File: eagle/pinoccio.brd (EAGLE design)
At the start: 25.4 x 50.8 mm, 71 parts, among them J1 AVR_SPI_PRG_6, J2 AVR_SPI, J3 Switch, J4 Ext Battery, Q1 PFET, U1 MCP73832, U2 TPS78233, U3 ATMEGA16U2, U4 ATMEGA256RFR2, U5 MAX17048, U6 SWITCH, U7 SWITCH, U8 LED-RGB, X1 16MHz, X2 32.768k, X3 16MHz, Y1 ANTENNA2SMD5

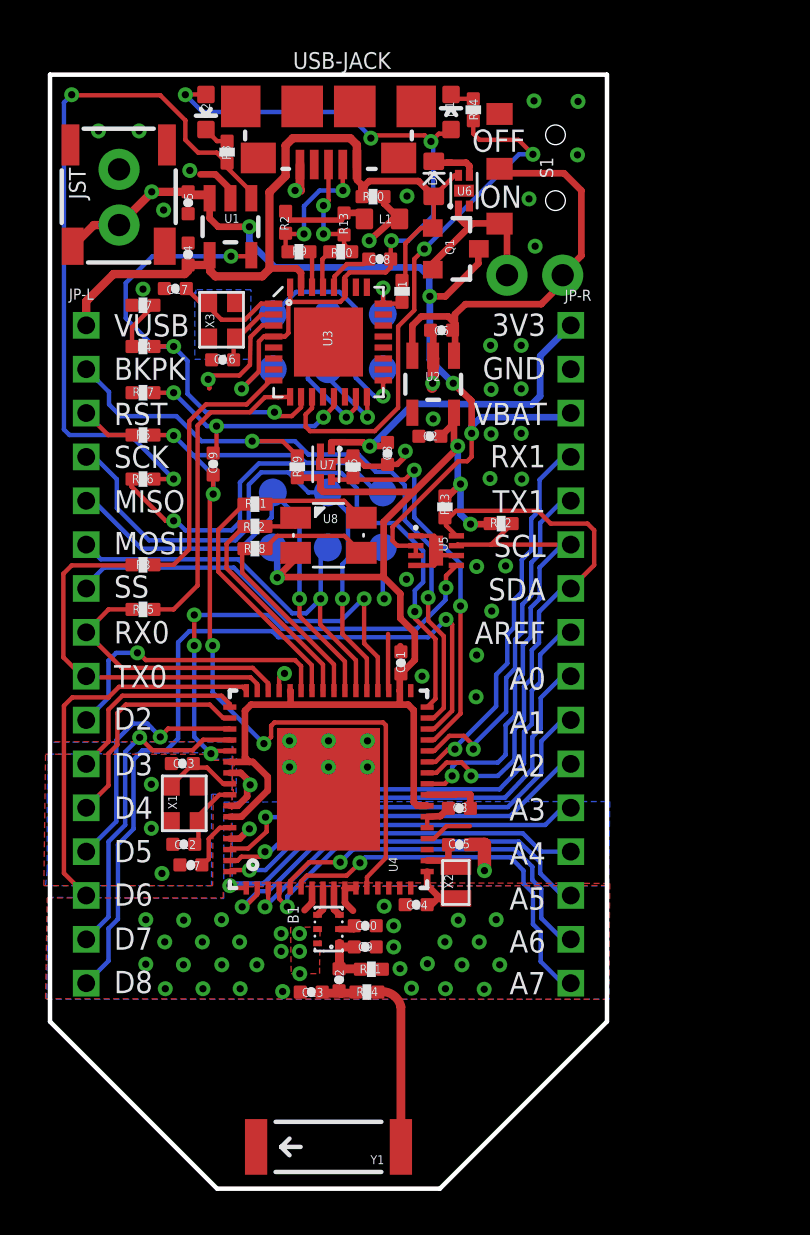
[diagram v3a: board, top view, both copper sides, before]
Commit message: Hardware updates to Scout v1.1
- Add 10k pull-up to reset line (#7)
- Add diode in parallel to 10k pull-up reset resistor (#6)
- Tie second pad on 16U2 crystal to ground (was not connected before)
- Replace LDO with lower-ripple alternative (#8) (STLQ015XX33)
- Add ground tie (0Ω) to pin 2 of balun
- Change all caps in RF signal path to RF-rated C0G/NPO (Murata GRM series)
- Reduce C7 and C8 to 100nF, and make C0G/NPO or X7R (<-Atmel engineer, could be 1.0µF instead)
- Consider adding the SE2438T Front-end module (FEM) amplifier
- Consider ferrite bead between digital and analog VDD lines
- Consider decoupling of 0.1µF on all VDD/GND pin pairs
- Move to a four layer board (GND/VDD in the middle two layers, signals on outer two)
- Add VBUS voltage check (with voltage divider to kick 5v -> 3.3v) into RFR2 and 16U2 input
- Change 16U2 to be powered via VBAT always, instead of off of VUSB
- Tie 16U2 pin to RFR2 pin, to notify RFR2 when serial port is opened
- Add series resistor to 16U2->RST line, removing existing reset circuit
- Remove load switch from VUSB, as it's now unneeded
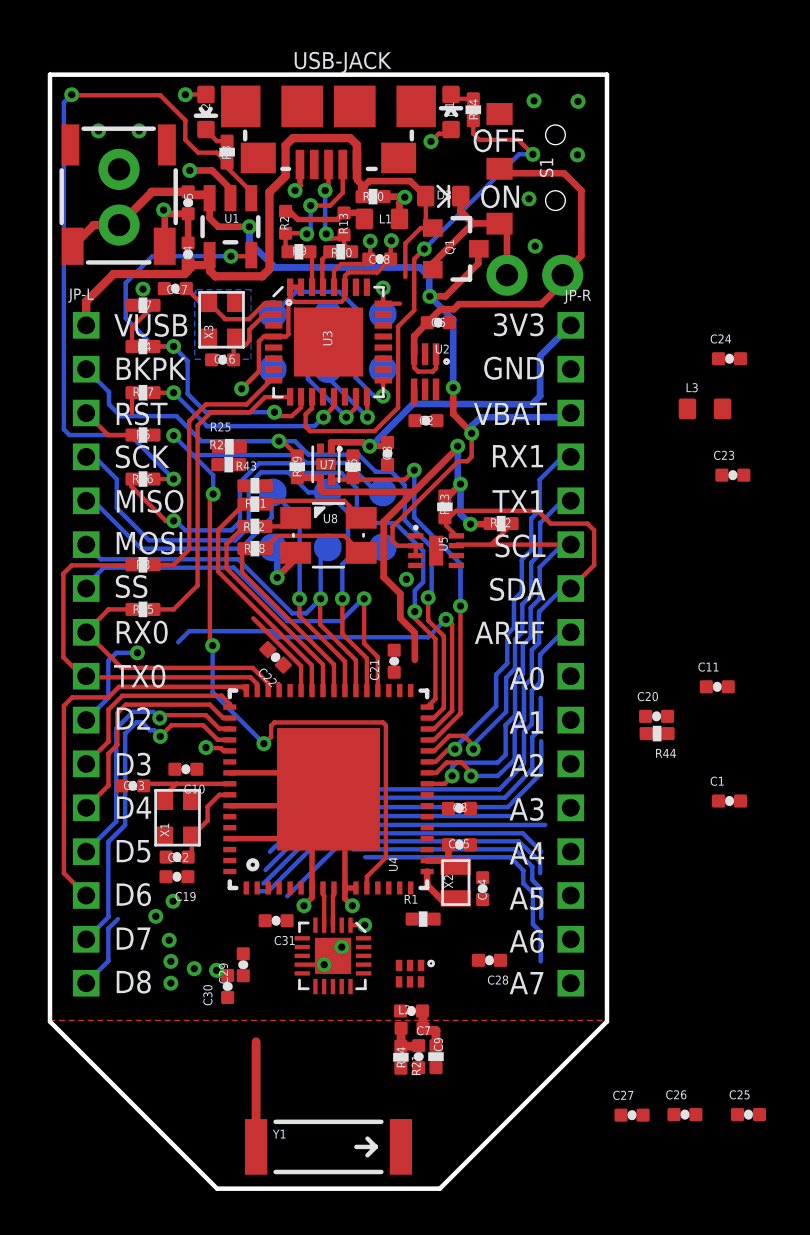
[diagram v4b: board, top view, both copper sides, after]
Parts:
- removed B1: BALUN, Pinoccio:BALUN
- removed U6: SWITCH, Pinoccio:TDFN4
- added C1, C20, C21, C22: 1.0uF, Pinoccio:0402-CAP
- added C24, C27, C28: 0.1uF, Pinoccio:0402-CAP
- added C25, C26, C31: 10pF, Pinoccio:0402-CAP
- added C29, C30: 22pF, Pinoccio:0402-CAP
- added L3: BEAD, Pinoccio:0603
- added R25: 68K, Pinoccio:0402-RES
- added R26: 100K, Pinoccio:0402-RES
- added R43: 1K, Pinoccio:0402-RES
- added R44: 10K, Pinoccio:0402-RES
- added U$17: SE2438T, Pinoccio:QFN-20-SE2438T
- added U$18: INVERTER-DUALPAK, Pinoccio:MICROPAK
- C10: value DNI -> 1.0uF
- C11: value 2.2uF -> 1.0uF
- C19: value 0.1uF -> 1.0uF
- C23: value 1.0pF -> 0.1uF
- C7: value 1.0uF -> 1.0pF
- JST: value (none) -> SFH
- L2: device Pinoccio:0402-CAP -> Pinoccio:0402
- R1: value 2K -> 2k
- R17: value 1K -> 10K
- U2: value TPS78233 -> STLQ015XX; device Pinoccio:SOT23-5 -> Pinoccio:SOT666
- moved C23 30.4 mm to (31.1, 32.5), turned to 0 degrees
- moved R1 28.6 mm to (17.0, 12.3), turned to 0 degrees
- moved C19 18.9 mm to (5.79, 14.2), turned to 180 degrees
- moved C11 14.5 mm to (30.4, 22.9), turned to 0 degrees
- moved C7 12.1 mm to (16.5, 8.10)
- moved C10 10.9 mm to (6.20, 19.1), turned to 180 degrees
- moved C9 5.57 mm to (16.8, 6.02), turned to 270 degrees
- moved R21 4.96 mm to (17.6, 6.02), turned to 90 degrees
- moved L2 3.99 mm to (16.5, 7.32), turned to 0 degrees
- moved R24 3.35 mm to (16.0, 5.99), turned to 270 degrees
- moved C14 3.12 mm to (19.7, 13.7), turned to 90 degrees
- moved C13 2.48 mm to (3.77, 18.4)
- moved U2 1.32 mm to (17.9, 37.9)
- moved D3 0.90 mm to (17.9, 45.3), turned to 0 degrees
- moved C2 0.73 mm to (17.1, 35.0)
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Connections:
- net N$15 renamed X1_P
- net N$16 renamed X1_N
- net N$19 renamed X3_N
- net N$2 renamed USBDIN_N
- net N$21 renamed X3_P
- net N$43 renamed USBDIN_P
- net USBD+ renamed USBD_P
- net USBD- renamed USBD_N
- removed net BATTALRT: U4.53, U5.P$5
- removed net N$13: B1.2, C10.1
- removed net N$20: C8.1, U4.21, U4.22
- removed net N$3: D3.C, U6.P$3
- removed net RFN: B1.3, U4.9
- removed net RFP: B1.4, U4.8
- removed net UCAP: C18.1, D1.A, D2.A, J1.2, U3.27, U3.32, U3.4
- removed net VUSB: C4.1, D3.A, JP-L.P$1, Q1.1, R1.1, R20.1, U1.4, U3.31, U6.P$4, USB-JACK.VBUS
- new net A0-IN: JP-R.P$9
- new net A1-IN: JP-R.P$10
- new net A2-IN: JP-R.P$11
- new net A3-IN: JP-R.P$12
- new net A4-IN: JP-R.P$13
- new net A5-IN: JP-R.P$14
- new net A6-IN: JP-R.P$15
- new net A7-IN: JP-R.P$16
- new net AGND: C31.2
- new net ANT: C7.1, L2.2, R21.2, U$17.13
- new net AVCC: C11.1, C23.1, C25.1, C26.1, C27.1, C28.1, C31.1, L3.1, U$17.1, U$17.19, U$17.2, U$17.6, U$18.P$5, U4.59
- new net AVDD: C19.1, U4.60
- new net CPS: U$17.8, U4.15
- new net CRX: C29.1, U$17.10, U$18.P$3, U$18.P$6
- new net CSD: U$17.12, U4.16
- new net CTX: C30.1, U$17.11, U$18.P$4
- new net DVDD: C1.1, C8.1, U4.21, U4.22
- new net RF_N: U$17.3, U4.9
- new net RF_P: U$17.4, U4.8
- new net RX/TX: R1.1, U4.14
- new net SEROPN: R43.1, U4.19
- new net VBUS: C4.1, D3.A, JP-L.P$1, Q1.1, R20.1, R25.1, U1.4, USB-JACK.VBUS
- new net VBUS-SENSE: R25.2, R26.2, U3.6, U4.53
- net A0: no longer JP-R.P$9
- net A1: no longer JP-R.P$10
- net A2: no longer JP-R.P$11
- net A3: no longer JP-R.P$12
- net A4: no longer JP-R.P$13
- net A5: no longer JP-R.P$14
- net A6: no longer JP-R.P$15
- net A7: no longer JP-R.P$16
- net GND: now also C1.2, C19.2, C20.2, C21.2, C22.2, C24.2, C25.2, C26.2, C27.2, C28.2, C29.2, C30.2, R21.1, R26.1, U$17.14, U$17.18, U$17.20, U$17.5, U$17.EP, U$17.P$1, U$17.P$2, U$18.P$2, U2.P$2; no longer B1.5, B1.6, R17.1, R21.2, U2.2, U2.4, U6.P$2, U6.P$5, X1.P$2, X1.P$4, X3.P$2, X3.P$4
- net N$10: now also R1.2, U$18.P$1; no longer C7.1, U4.60
- net N$24: no longer C19.2
- net N$27: now also C9.1, L2.1; no longer C23.1, L2.2
- net N$4: now also R43.2, U3.12; no longer B1.1, C9.1, L2.1, R21.1
- net N$51: now also D3.C; no longer U6.P$1
- net N$7: now also R44.1; no longer R1.2
- net RESET: now also R17.1; no longer C19.1
- net VCC: now also C10.1, C18.1, C20.1, C21.1, C22.1, C24.1, D1.A, D2.A, J1.2, L3.2, R44.2, U2.P$4, U3.27, U3.31, U3.32, U3.4; no longer C11.1, U2.5, U4.59
- net VIN: now also U2.P$1, U2.P$3; no longer U2.1, U2.3
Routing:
- net VUSB: track 37.4 -> 0.00 mm
- net UCAP: track 35.2 -> 0.00 mm, vias 5 -> 0
- net VBUS: track 0.00 -> 33.5 mm
- net BATTALRT: track 21.6 -> 0.00 mm, vias 4 -> 0
- net D8: track 36.6 -> 22.2 mm
- net VCC: track 57.4 -> 44.2 mm, vias 4 -> 8
- net A4: track 16.6 -> 9.56 mm
- net A2: track 18.6 -> 12.5 mm
- net A6: track 16.5 -> 11.0 mm
- net A7: track 17.4 -> 11.9 mm, vias 1 -> 0
- net GND: track 46.7 -> 41.3 mm, vias 79 -> 16
- net D2: track 13.5 -> 8.85 mm
- net AREF: track 22.6 -> 18.7 mm
- net A0: track 20.7 -> 16.9 mm
- net A3: track 18.1 -> 14.3 mm
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- added copper zone on layer 2, net GND
- added copper zone on layer 1, net N$2
- added copper zone on layer 15, net VCC
- removed copper zone on layer 1, net GND
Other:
- board text added: "Pinoccio(tm) v1.1"
- board text added: "pinoccio v1.1"
- board text removed: "Pinoccio(tm) v1.0"
- board text removed: "pinoccio v1.0"

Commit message: Add caps to FEM
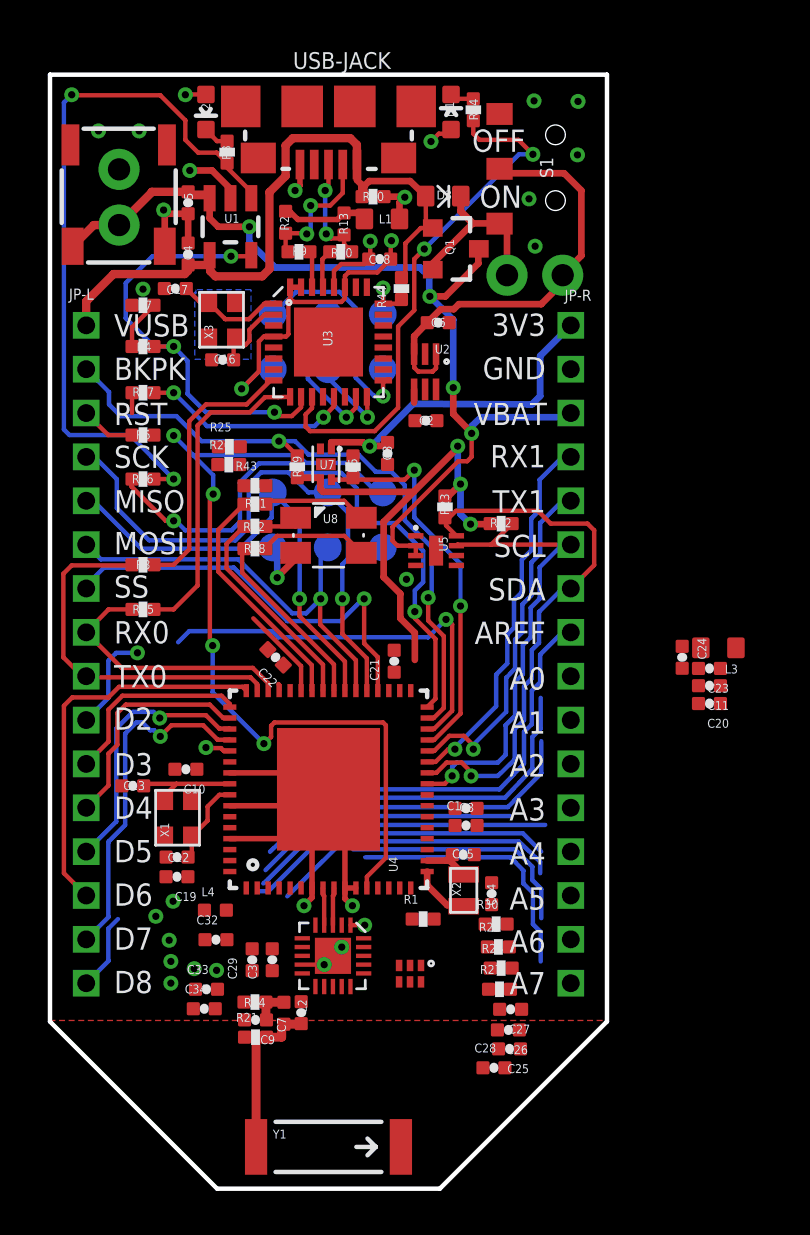
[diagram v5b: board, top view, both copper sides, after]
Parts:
- removed C31: 10pF, Pinoccio:0402-CAP
- added C32, C33: 0.1uF, Pinoccio:0402-CAP
- added C34: 10pF, Pinoccio:0402-CAP
- added L4: 3.6nH, Pinoccio:0402
- added R27, R28, R29, R30: 100K, Pinoccio:0402-RES
- moved R44 23.4 mm to (16.0, 41.0), turned to 90 degrees
- moved C24 13.8 mm to (28.8, 24.2), turned to 270 degrees
- moved C1 12.1 mm to (19.0, 16.6)
- moved C25 11.3 mm to (21.0, 6.38), turned to 180 degrees
- moved L3 10.9 mm to (30.5, 24.7), turned to 180 degrees
- moved C26 8.93 mm to (20.9, 7.24), turned to 180 degrees
- moved C23 8.88 mm to (30.1, 23.7), turned to 180 degrees
- moved R21 8.28 mm to (9.37, 6.91), turned to 0 degrees
- moved C9 7.63 mm to (9.37, 7.70), turned to 180 degrees
- moved C27 7.35 mm to (21.0, 8.18), turned to 180 degrees
- moved R24 7.11 mm to (9.35, 8.51), turned to 180 degrees
- moved L2 5.88 mm to (10.7, 8.00), turned to 270 degrees
- moved C7 5.03 mm to (11.5, 8.03), turned to 90 degrees
- moved C28 4.91 mm to (20.2, 5.51), turned to 0 degrees
- moved C20 2.48 mm to (30.1, 22.1), turned to 180 degrees
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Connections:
- new net N$3: L4.2, U$17.19
- net AGND: now also C33.2, C34.2; no longer C31.2
- net AVCC: now also C32.1, C33.1, C34.1, L4.1; no longer C31.1, U$17.19, U$17.2
- net AVDD: now also U$17.2
- net CPS: now also R30.1
- net CRX: now also R27.1
- net CSD: now also R28.1
- net CTX: now also R29.1
- net GND: now also C32.2, R27.2, R28.2, R29.2, R30.2

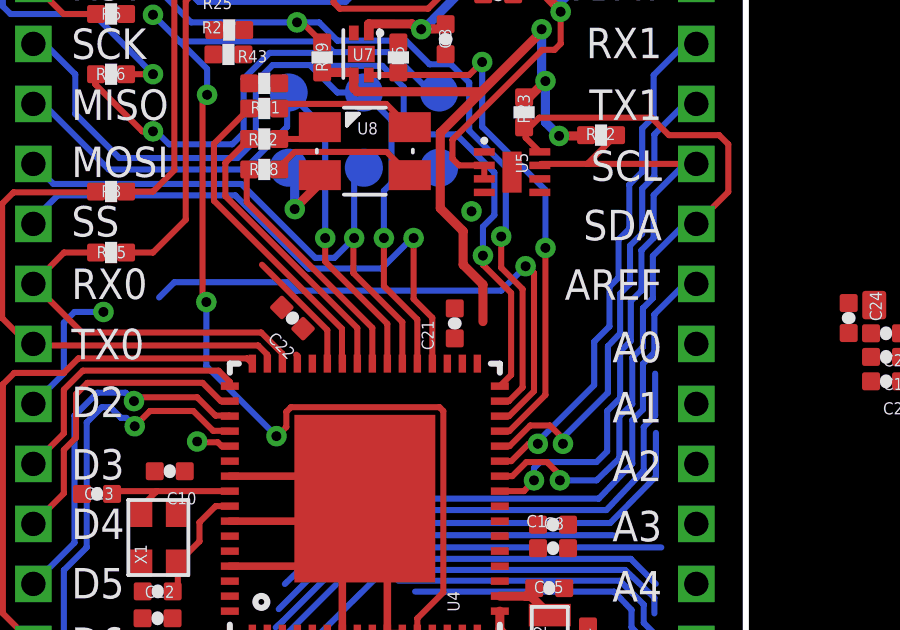
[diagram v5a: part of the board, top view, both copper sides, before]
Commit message: Change 256RFR2 decoupling to 0.1µF and add single 1.0µF for transient current draw
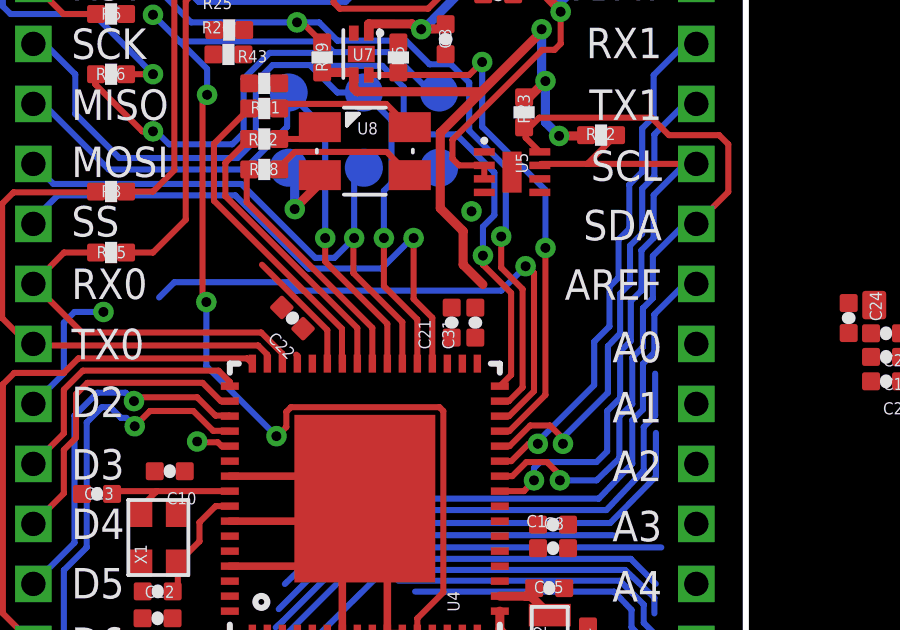
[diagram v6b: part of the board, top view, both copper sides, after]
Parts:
- added C31: 1.0uF, Pinoccio:0402-CAP
- C1, C10, C11, C19, C20, C21, C22, C8: value 1.0uF -> 0.1uF
- moved C21 0.10 mm to (15.6, 24.1)
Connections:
- net GND: now also C31.2
- net VCC: now also C31.1
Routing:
- net VCC: track 44.2 -> 43.0 mm

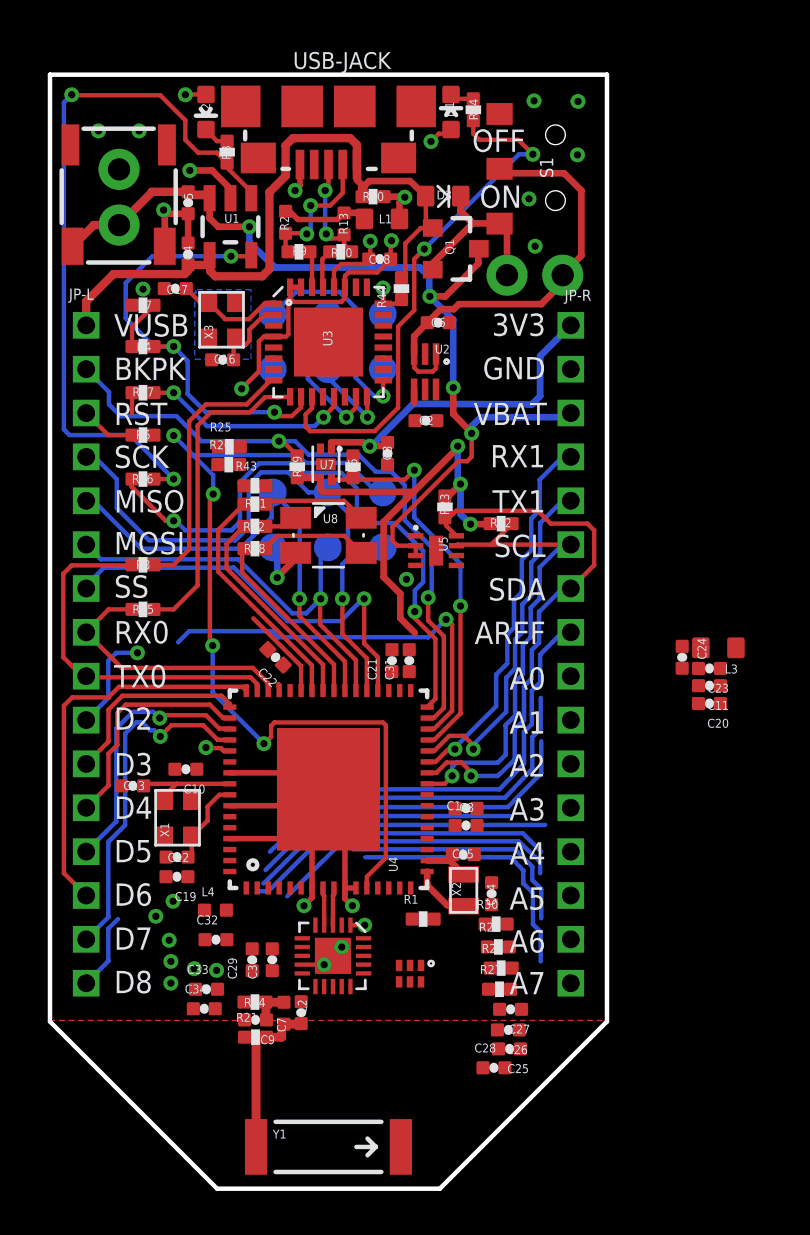
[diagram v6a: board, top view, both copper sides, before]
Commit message: Clean up labels and fix bypass/decoupling caps
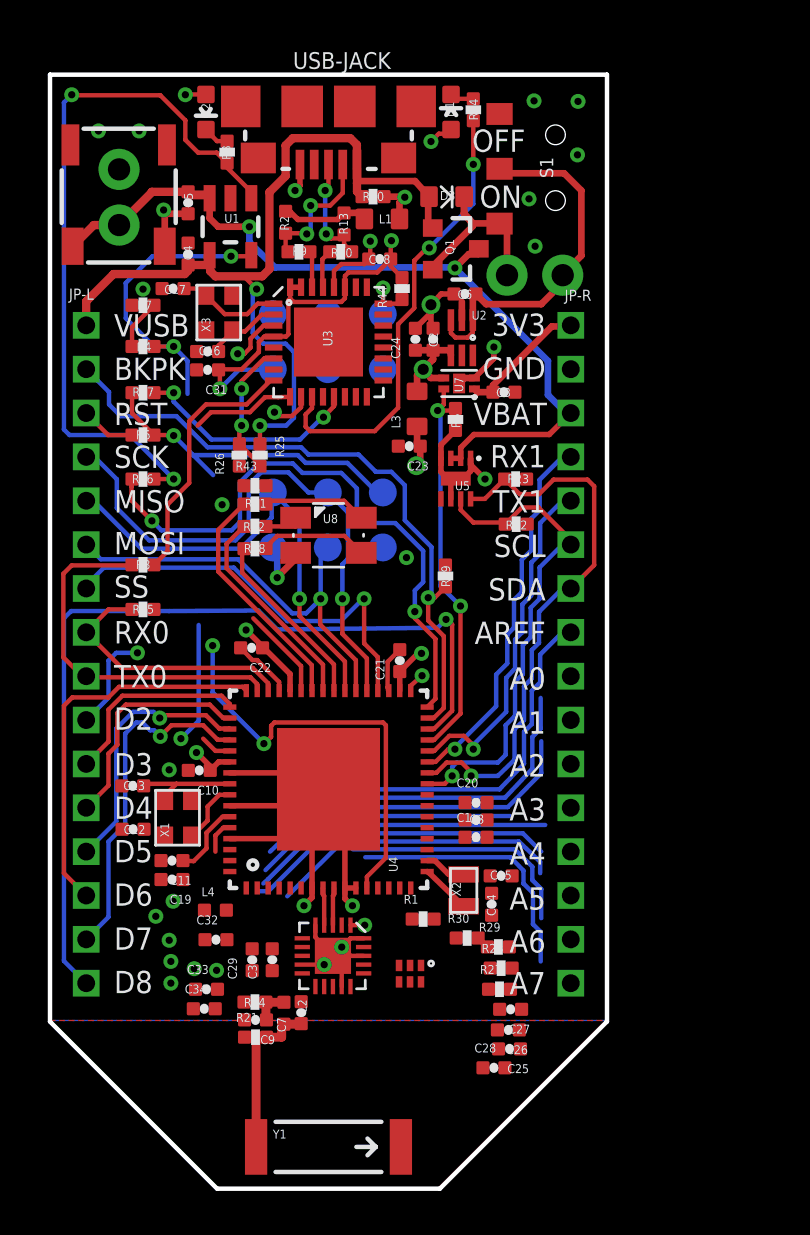
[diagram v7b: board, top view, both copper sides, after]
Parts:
- C1, C10, C11, C19, C20, C21, C22, C8: value 0.1uF -> 1.0uF
- C31: value 1.0uF -> 0.1uF
- D1: value Green -> (Green)
- moved C11 25.8 mm to (5.56, 15.0)
- moved C24 18.9 mm to (16.7, 38.7), turned to 90 degrees
- moved L3 17.5 mm to (16.7, 35.6), turned to 90 degrees
- moved C23 17.0 mm to (16.4, 33.9)
- moved C31 16.1 mm to (7.19, 37.3), turned to 180 degrees
- moved C20 11.6 mm to (19.4, 17.6), turned to 0 degrees
- moved R19 8.39 mm to (18.0, 27.9), turned to 270 degrees
- moved U7 6.68 mm to (19.5, 36.1), turned to 90 degrees
- moved C3 6.00 mm to (20.7, 36.3), turned to 0 degrees
- moved R5 5.15 mm to (18.5, 35.1), turned to 270 degrees
- moved U5 4.79 mm to (19.3, 33.7), turned to 180 degrees
- moved C2 3.73 mm to (17.5, 38.7), turned to 90 degrees
- moved R23 3.47 mm to (21.2, 32.4), turned to 180 degrees
- moved C12 2.37 mm to (3.79, 16.4)
- moved U2 2.28 mm to (19.6, 39.5)
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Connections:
- net N$56 renamed 16U2-MISO
- net N$57 renamed 16U2-MOSI
- net N$58 renamed 16U2-SCK
- net N$7 renamed 16U2-RESET
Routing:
- net GND: track 41.3 -> 64.3 mm, vias 16 -> 21
- net D8: track 22.2 -> 41.0 mm
- net VBUS-SENSE: track 1.20 -> 13.2 mm, vias 1 -> 3
- net 16U2-MISO: track 11.0 -> 0.00 mm, vias 1 -> 0
- net N$25: track 14.5 -> 4.76 mm
- net VCC-AE: track 15.6 -> 5.90 mm, vias 1 -> 0
- net VBUS: track 33.5 -> 41.6 mm, vias 0 -> 2
- net 16U2-SCK: track 7.40 -> 0.00 mm, vias 1 -> 0
- net VCC: track 43.0 -> 36.0 mm, vias 8 -> 9
- net VBAT: track 44.7 -> 38.0 mm, vias 4 -> 2
- net RESET: track 40.3 -> 34.9 mm
- net AVCC: track 0.65 -> 5.96 mm, vias 1 -> 2
- net PROG: track 20.1 -> 15.8 mm
- net 16U2-MOSI: track 4.12 -> 0.00 mm, vias 1 -> 0
- net N$59: track 24.4 -> 20.8 mm
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- added copper zone on layer 16, net N$12
- removed copper zone on layer 16, net GND
